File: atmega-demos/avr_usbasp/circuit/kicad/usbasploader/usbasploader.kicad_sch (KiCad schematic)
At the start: 21 parts, among them J1 Conn_01x06_Pin, J2 USB_B_Mini, SW1 SW_Push, SW2 SW_Push, U1 ATmega8A-A, Y1 12MHz

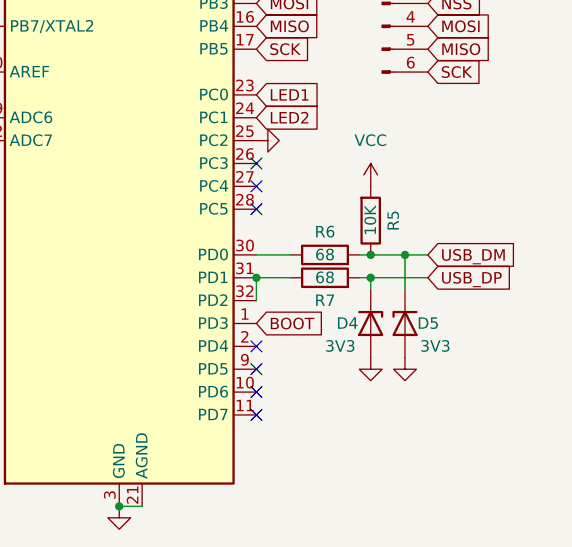
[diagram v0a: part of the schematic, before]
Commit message: USBAsp KiCAD
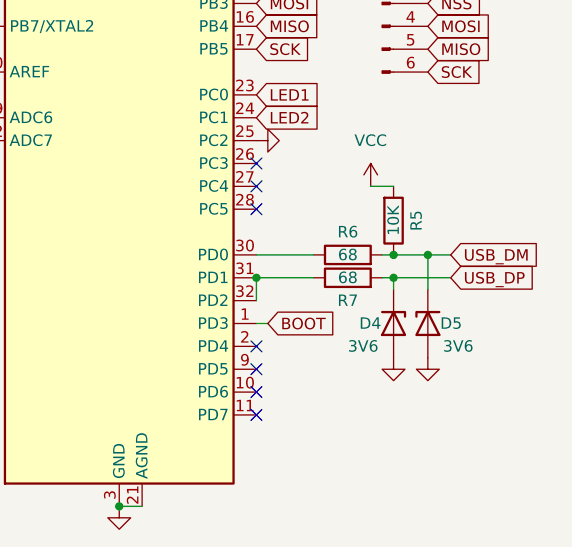
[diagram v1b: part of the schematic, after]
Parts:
- D4, D5: value 3V3 -> 3V6
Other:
- moved on the sheet: D4, D5, R5, R6, R7

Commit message: USBASP Loader PCB
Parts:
- added C1: 100n, Capacitor_SMD:C_0805_2012Metric_Pad1.18x1.45mm_HandSolder, symbol Device:C
- renumbered C1 to C2, C2 to C3
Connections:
- net GND: now also C1.1
- net VCC: now also C1.2
